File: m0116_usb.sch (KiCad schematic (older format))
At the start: 20 parts, among them J1 AVR-ISP-6, J2 USB_B_Mini, U1 ATmega32A-PU, Y1 16Mhz

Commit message: finished
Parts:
- removed D82: LED, LED_THT:LED_D3.0mm, symbol Device:LED
- removed R4: 1.5k, Resistor_THT:R_Axial_DIN0207_L6.3mm_D2.5mm_P10.16mm_Horizontal, symbol Device:R
- added D10, D11, D12, D13, D14, D15, D16, D17, D18, D19, D20, D21, D22, D23, D24, D25, D26, D27, D28, D29, D3, D30, D31, D32, D33, D34, D35, D36, D37, D38, D39, D4, D40, D41, D42, D43, D44, D45, D46, D47, D48, D49, D5, D50, D51, D52, D53, D54, D55, D56, D57, D58, D59, D6, D60, D61, D62, D63, D64, D65, D66, D67, D68, D69, D7, D70, D71, D72, D73, D74, D75, D76, D77, D78, D79, D8, D80, D81, D83, D84, D9: D_Small, Diode_THT:D_DO-35_SOD27_P7.62mm_Horizontal, symbol Device:D_Small
- added J3, J4: Conn_01x04, Connector_PinHeader_2.54mm:PinHeader_1x04_P2.54mm_Vertical, symbol Connector_Generic:Conn_01x04
- added J5, J6: Conn_01x06, Connector_PinHeader_2.54mm:PinHeader_1x06_P2.54mm_Vertical, symbol Connector_Generic:Conn_01x06
- added MX1, MX10, MX11, MX12, MX13, MX14, MX15, MX16, MX17, MX18, MX19, MX2, MX20, MX21, MX22, MX23, MX24, MX25, MX26, MX27, MX28, MX29, MX3, MX30, MX31, MX32, MX33, MX34, MX35, MX36, MX37, MX38, MX39, MX4, MX40, MX41, MX42, MX43, MX44, MX45, MX46, MX47, MX48, MX49, MX5, MX50, MX51, MX52, MX53, MX54, MX55, MX56, MX57, MX58, MX59, MX6, MX60, MX61, MX62, MX63, MX64, MX65, MX66, MX67, MX68, MX69, MX7, MX70, MX71, MX72, MX73, MX74, MX75, MX76, MX77, MX78, MX79, MX8, MX80, MX81, MX9: MX-NoLED, Alps_Only:ALPS-1U, symbol MX_Alps_Hybrid:MX-NoLED
- F1: footprint custom_parts:Fuse_Littelfuse_395Series -> Fuse:Fuse_Littelfuse_395Series
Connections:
- net +5V: now also R5.2, J3.1 (Pin_1), J4.1 (Pin_1), J5.6 (Pin_6), J6.6 (Pin_6); no longer R5.1
- net D+: now also R3.2; no longer R2.2
- net D-: now also R2.2; no longer R3.2
- net GND: now also J3.4 (Pin_4), J4.4 (Pin_4), J5.1 (Pin_1), J6.1 (Pin_1)
- net MISO: now also J6.4 (Pin_4); no longer J1.1 (MISO)
- net MOSI: now also J6.5 (Pin_5); no longer J1.4 (MOSI)
- net SCK: now also J6.3 (Pin_3); no longer J1.3 (SCK)
- net reset: now also J6.2 (Pin_2); no longer J1.5 (~RST)
- net col4: now reaches U1.14 (PD0)
- net col4: now also MX22.1 (COL), MX4.1 (COL), MX40.1 (COL), MX56.1 (COL), MX71.1 (COL)
- net col3: now reaches U1.15 (PD1)
- net col3: now also MX21.1 (COL), MX3.1 (COL), MX39.1 (COL), MX55.1 (COL), MX70.1 (COL)
- net col2: now reaches U1.19 (PD5)
- net col2: now also MX2.1 (COL), MX20.1 (COL), MX38.1 (COL), MX54.1 (COL), MX69.1 (COL)
- net row0: now reaches U1.2 (PB1)
- net row0: now also D10.1 (K), D11.1 (K), D12.1 (K), D13.1 (K), D14.1 (K), D15.1 (K), D16.1 (K), D17.1 (K), D18.1 (K), D19.1 (K), D20.1 (K), D3.1 (K), D4.1 (K), D5.1 (K), D6.1 (K), D7.1 (K), D8.1 (K), D9.1 (K)
- net col1: now reaches U1.20 (PD6)
- net col1: now also MX1.1 (COL), MX19.1 (COL), MX37.1 (COL), MX53.1 (COL), MX68.1 (COL)
- net col5: now reaches U1.21 (PD7)
- net col5: now also MX23.1 (COL), MX41.1 (COL), MX5.1 (COL), MX57.1 (COL)
- net col6: now reaches U1.22 (PC0)
- net col6: now also MX24.1 (COL), MX42.1 (COL), MX58.1 (COL), MX6.1 (COL), MX81.1 (COL)
- net col7: now reaches U1.23 (PC1)
- net col7: now also MX25.1 (COL), MX43.1 (COL), MX59.1 (COL), MX7.1 (COL)
- net col8: now reaches U1.24 (PC2)
- net col8: now also MX26.1 (COL), MX44.1 (COL), MX60.1 (COL), MX72.1 (COL), MX8.1 (COL)
- net col9: now reaches U1.25 (PC3)
- net col9: now also MX27.1 (COL), MX45.1 (COL), MX61.1 (COL), MX73.1 (COL), MX9.1 (COL)
- net col10: now reaches U1.26 (PC4)
- net col10: now also MX10.1 (COL), MX28.1 (COL), MX46.1 (COL), MX62.1 (COL), MX74.1 (COL)
- net col11: now reaches U1.27 (PC5)
- net col11: now also MX11.1 (COL), MX29.1 (COL), MX47.1 (COL), MX63.1 (COL), MX75.1 (COL)
- net col12: now reaches U1.28 (PC6)
- net col12: now also MX12.1 (COL), MX30.1 (COL), MX48.1 (COL), MX76.1 (COL)
- net col13: now reaches U1.29 (PC7)
- net col13: now also MX13.1 (COL), MX31.1 (COL)
- net row2: now reaches U1.3 (PB2)
- net row2: now also D39.1 (K), D40.1 (K), D41.1 (K), D42.1 (K), D43.1 (K), D44.1 (K), D45.1 (K), D46.1 (K), D47.1 (K), D48.1 (K), D49.1 (K), D50.1 (K), D51.1 (K), D52.1 (K), D53.1 (K), D54.1 (K)
- net col14: now reaches U1.33 (PA7)
- net col14: now also MX14.1 (COL), MX32.1 (COL), MX64.1 (COL), MX77.1 (COL)
- net col15: now reaches U1.34 (PA6)
- net col15: now also MX15.1 (COL), MX33.1 (COL), MX49.1 (COL), MX65.1 (COL), MX78.1 (COL)
- net col16: now reaches U1.35 (PA5)
- net col16: now also MX16.1 (COL), MX34.1 (COL), MX50.1 (COL), MX66.1 (COL)
- net col17: now reaches U1.36 (PA4)
- net col17: now also MX17.1 (COL), MX35.1 (COL), MX51.1 (COL), MX67.1 (COL), MX79.1 (COL)
- net col18: now reaches U1.37 (PA3)
- net col18: now also MX18.1 (COL), MX36.1 (COL), MX52.1 (COL), MX80.1 (COL)
- net row3: now reaches U1.38 (PA2)
- net row3: now also D55.1 (K), D56.1 (K), D57.1 (K), D58.1 (K), D59.1 (K), D60.1 (K), D61.1 (K), D62.1 (K), D63.1 (K), D64.1 (K), D65.1 (K), D66.1 (K), D67.1 (K), D68.1 (K), D69.1 (K)
- net row4: now reaches U1.39 (PA1)
- net row4: now also D70.1 (K), D71.1 (K), D72.1 (K), D73.1 (K), D74.1 (K), D75.1 (K), D76.1 (K), D77.1 (K), D78.1 (K), D79.1 (K), D80.1 (K), D81.1 (K), D83.1 (K), D84.1 (K)
- net row1: now reaches U1.40 (PA0)
- net row1: now also D21.1 (K), D22.1 (K), D23.1 (K), D24.1 (K), D25.1 (K), D26.1 (K), D27.1 (K), D28.1 (K), D29.1 (K), D30.1 (K), D31.1 (K), D32.1 (K), D33.1 (K), D34.1 (K), D35.1 (K), D36.1 (K), D37.1 (K), D38.1 (K)
- net at D2.1 (K), J2.2 (D-): now also J4.3 (Pin_3); no longer R3.1
- net at D1.1 (K), J2.3 (D+): now also J4.2 (Pin_2); no longer R2.1, R5.2
- new net: J3.2 (Pin_2), R3.1
- new net: J3.3 (Pin_3), R2.1, R5.1
- new net: D3.2 (A), MX1.2 (ROW)
- new net: D4.2 (A), MX2.2 (ROW)
- new net: D5.2 (A), MX3.2 (ROW)
- new net: D6.2 (A), MX4.2 (ROW)
- new net: D7.2 (A), MX5.2 (ROW)
- new net: D8.2 (A), MX6.2 (ROW)
- new net: D9.2 (A), MX7.2 (ROW)
- new net: D10.2 (A), MX8.2 (ROW)
- new net: D11.2 (A), MX9.2 (ROW)
- new net: D12.2 (A), MX10.2 (ROW)
- new net: D13.2 (A), MX11.2 (ROW)
- new net: D14.2 (A), MX12.2 (ROW)
- new net: D15.2 (A), MX13.2 (ROW)
- new net: D16.2 (A), MX14.2 (ROW)
- new net: D17.2 (A), MX15.2 (ROW)
- new net: D18.2 (A), MX16.2 (ROW)
- new net: D19.2 (A), MX17.2 (ROW)
- new net: D20.2 (A), MX18.2 (ROW)
- new net: D21.2 (A), MX19.2 (ROW)
- new net: D22.2 (A), MX20.2 (ROW)
- new net: D23.2 (A), MX21.2 (ROW)
- new net: D24.2 (A), MX22.2 (ROW)
- new net: D25.2 (A), MX23.2 (ROW)
- new net: D26.2 (A), MX24.2 (ROW)
- new net: D27.2 (A), MX25.2 (ROW)
- new net: D28.2 (A), MX26.2 (ROW)
- new net: D29.2 (A), MX27.2 (ROW)
- new net: D30.2 (A), MX28.2 (ROW)
- new net: D31.2 (A), MX29.2 (ROW)
- new net: D32.2 (A), MX30.2 (ROW)
- new net: D33.2 (A), MX31.2 (ROW)
- new net: D34.2 (A), MX32.2 (ROW)
- new net: D35.2 (A), MX33.2 (ROW)
- new net: D36.2 (A), MX34.2 (ROW)
- new net: D37.2 (A), MX35.2 (ROW)
- new net: D38.2 (A), MX36.2 (ROW)
- new net: D39.2 (A), MX37.2 (ROW)
- new net: D40.2 (A), MX38.2 (ROW)
- new net: D41.2 (A), MX39.2 (ROW)
- new net: D42.2 (A), MX40.2 (ROW)
- new net: D43.2 (A), MX41.2 (ROW)
- new net: D44.2 (A), MX42.2 (ROW)
- new net: D45.2 (A), MX43.2 (ROW)
- new net: D46.2 (A), MX44.2 (ROW)
- new net: D47.2 (A), MX45.2 (ROW)
- new net: D48.2 (A), MX46.2 (ROW)
- new net: D49.2 (A), MX47.2 (ROW)
- new net: D50.2 (A), MX48.2 (ROW)
- new net: D51.2 (A), MX49.2 (ROW)
- new net: D52.2 (A), MX50.2 (ROW)
- new net: D53.2 (A), MX51.2 (ROW)
- new net: D54.2 (A), MX52.2 (ROW)
- new net: D55.2 (A), MX53.2 (ROW)
- new net: D56.2 (A), MX54.2 (ROW)
- new net: D57.2 (A), MX55.2 (ROW)
- new net: D58.2 (A), MX56.2 (ROW)
- new net: D59.2 (A), MX57.2 (ROW)
- new net: D60.2 (A), MX58.2 (ROW)
- new net: D61.2 (A), MX59.2 (ROW)
- new net: D62.2 (A), MX60.2 (ROW)
- new net: D63.2 (A), MX61.2 (ROW)
- new net: D64.2 (A), MX62.2 (ROW)
- new net: D65.2 (A), MX63.2 (ROW)
- new net: D66.2 (A), MX64.2 (ROW)
- new net: D67.2 (A), MX65.2 (ROW)
- new net: D68.2 (A), MX66.2 (ROW)
- new net: D69.2 (A), MX67.2 (ROW)
- new net: D70.2 (A), MX68.2 (ROW)
- new net: D71.2 (A), MX69.2 (ROW)
- new net: D72.2 (A), MX70.2 (ROW)
- new net: D73.2 (A), MX71.2 (ROW)
- new net: D74.2 (A), MX72.2 (ROW)
- new net: D75.2 (A), MX73.2 (ROW)
- new net: D76.2 (A), MX74.2 (ROW)
- new net: D77.2 (A), MX75.2 (ROW)
- new net: D78.2 (A), MX76.2 (ROW)
- new net: D79.2 (A), MX77.2 (ROW)
- new net: D80.2 (A), MX78.2 (ROW)
- new net: D81.2 (A), MX79.2 (ROW)
- new net: D83.2 (A), MX80.2 (ROW)
- new net: D84.2 (A), MX81.2 (ROW)
- new net: J1.1 (MISO), J5.4 (Pin_4)
- new net: J1.3 (SCK), J5.3 (Pin_3)
- new net: J1.4 (MOSI), J5.5 (Pin_5)
- new net: J1.5 (~RST), J5.2 (Pin_2)
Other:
- moved on the sheet: F1, R2, R3, R5

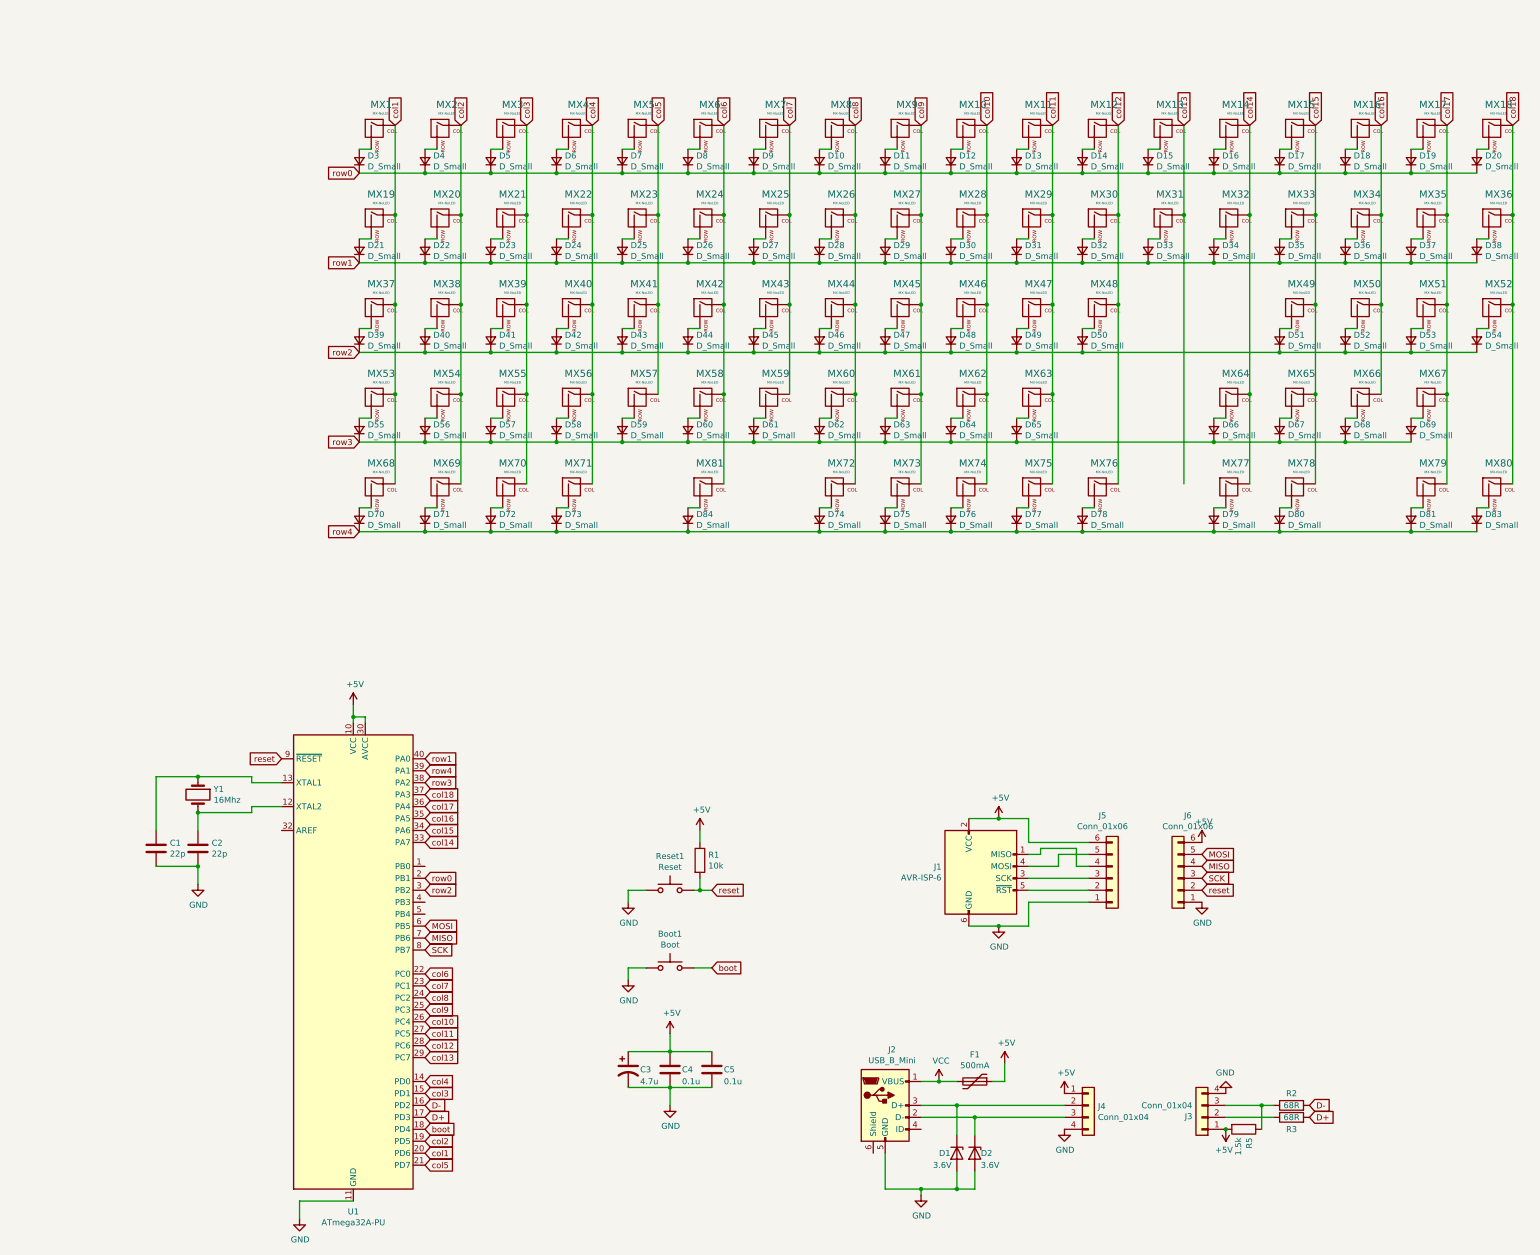
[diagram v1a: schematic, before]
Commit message: fix wrong resistor connection
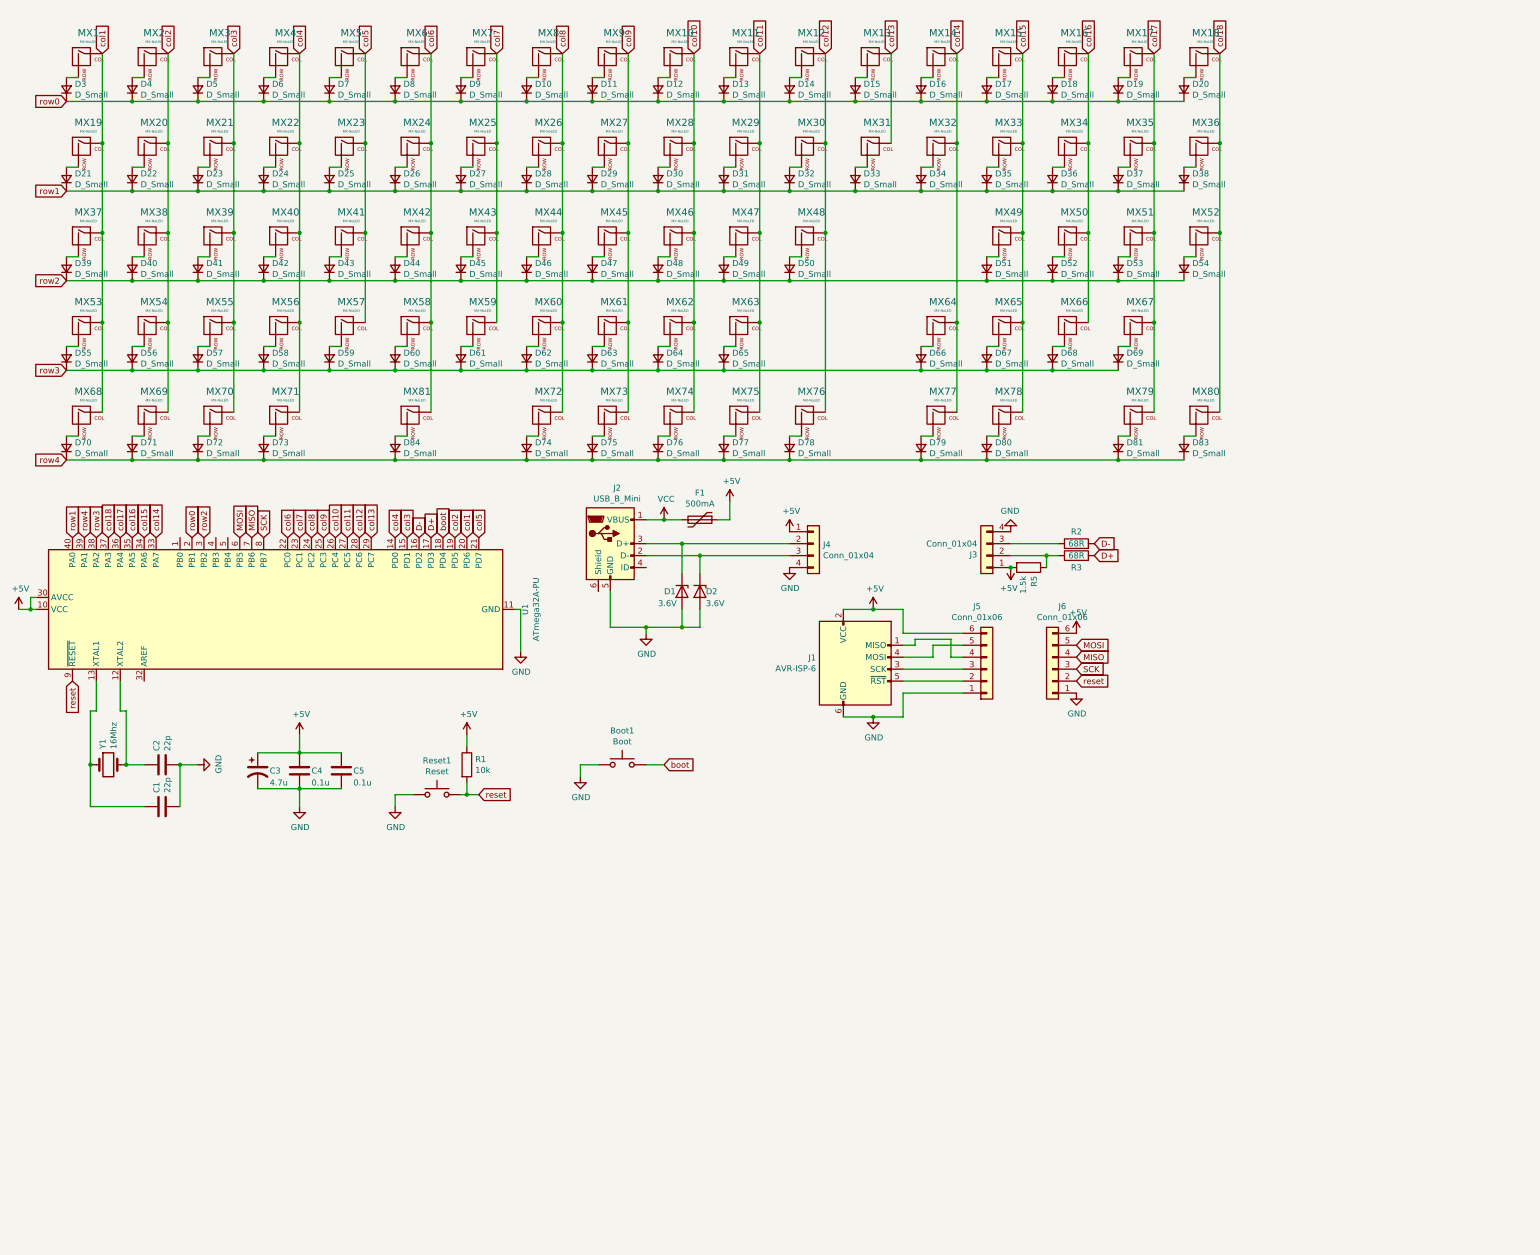
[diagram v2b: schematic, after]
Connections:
- net at J3.2 (Pin_2), R3.1: now also R5.1
- net at J3.3 (Pin_3), R2.1: no longer R5.1
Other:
- moved on the sheet: Boot1, C1, C2, C3, C4, C5, D1, D10, D11, D12, D13, D14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

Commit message: rev1
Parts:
- removed C1, C2: 22p, Capacitor_THT:C_Disc_D6.0mm_W2.5mm_P5.00mm, symbol Device:C
- removed J5, J6: Conn_01x06, Connector_PinHeader_2.54mm:PinHeader_1x06_P2.54mm_Vertical, symbol Connector_Generic:Conn_01x06
- removed Y1: 16Mhz, Crystal:Crystal_HC49-4H_Vertical, symbol Device:Crystal
- added Y1: Resonator, Crystal:Resonator-3Pin_W7.0mm_H2.5mm, symbol Device:Resonator
- renumbered C3 to C1, C4 to C2, C5 to C3, D84 to D74, D74 to D75, D75 to D76, D76 to D77, D77 to D78, D78 to D79, D79 to D80, D80 to D81, D81 to D82, J4 to J2, MX81 to MX72, MX72 to MX73, MX73 to MX74, MX74 to MX75, MX75 to MX76, MX76 to MX77, MX77 to MX78, MX78 to MX79, MX79 to MX80, MX80 to MX81, R5 to R2, R2 to R4, J2 to USB1
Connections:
- net D+: now also U1.16 (PD2); no longer U1.17 (PD3)
- net D-: now also U1.17 (PD3); no longer U1.16 (PD2)
- net GND: now also USB1.6 (Shield), Y1.2
- net MISO: now also J1.1 (MISO)
- net MOSI: now also J1.4 (MOSI)
- net SCK: now also J1.3 (SCK)
- net reset: now also J1.5 (~RST)
- net at U1.12 (XTAL2): now also Y1.3
- net at U1.13 (XTAL1): now also Y1.1
- net at J3.2 (Pin_2), R3.1: no longer R2.1
- net at J3.3 (Pin_3), R4.1: now also R2.1
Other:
- moved on the sheet: J1, J3, R2, R3, R4

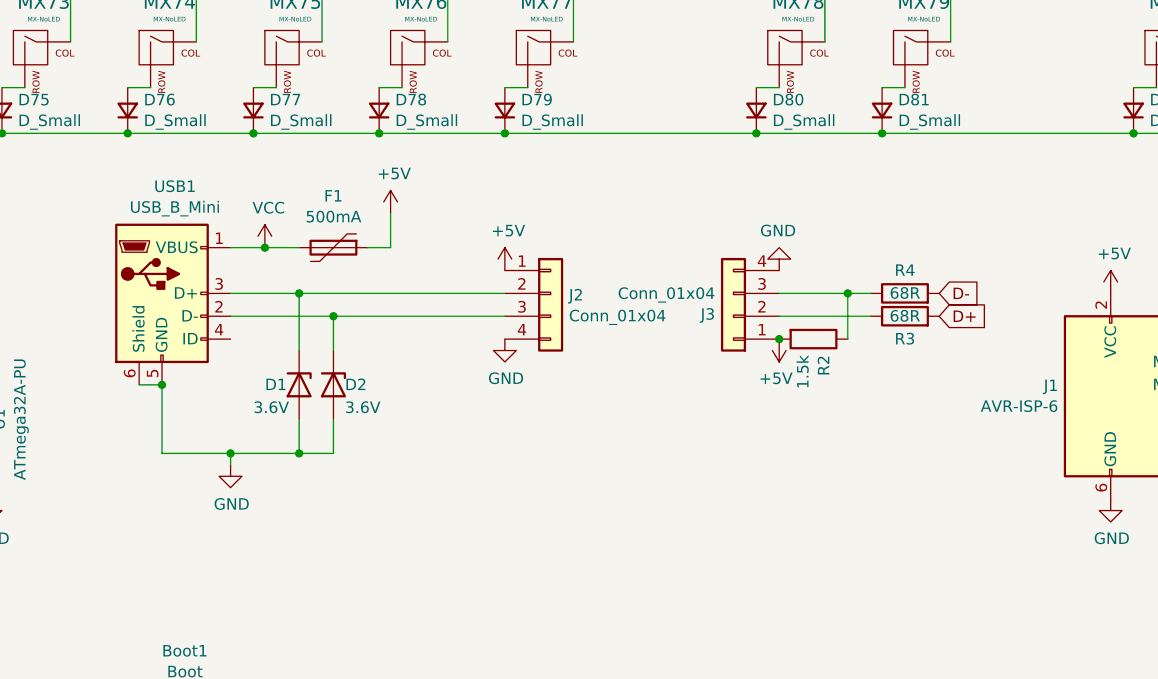
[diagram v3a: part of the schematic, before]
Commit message: change design of daughterboard
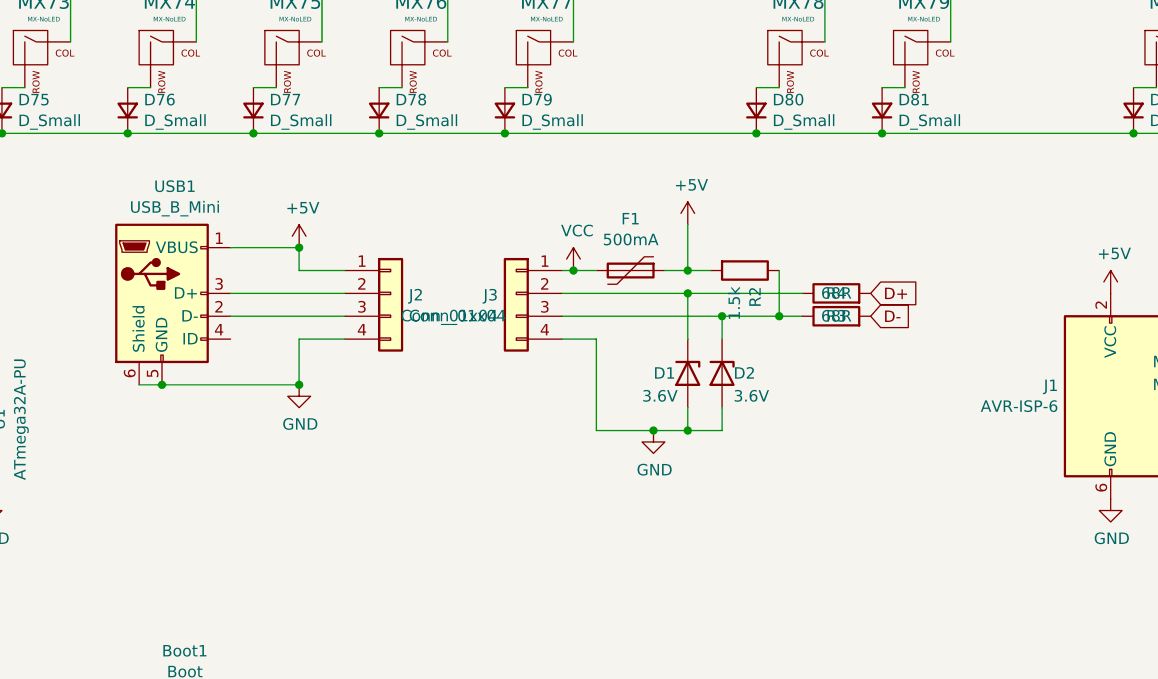
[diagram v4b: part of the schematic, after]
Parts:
- J2: footprint Connector_PinHeader_2.54mm:PinHeader_1x04_P2.54mm_Vertical -> Connector_PinHeader_2.00mm:PinHeader_1x04_P2.00mm_Vertical
- J3: footprint Connector_PinHeader_2.54mm:PinHeader_1x04_P2.54mm_Vertical -> Connector_JST:JST_EH_B4B-EH-A_1x04_P2.50mm_Vertical
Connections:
- net +5V: now also USB1.1 (VBUS); no longer J3.1 (Pin_1)
- net VCC: now also J3.1 (Pin_1); no longer USB1.1 (VBUS)
- net at J3.2 (Pin_2), R3.1: now also D1.1 (K)
- net at J3.3 (Pin_3), R2.1, R4.1: now also D2.1 (K)
- net at J2.2 (Pin_2), USB1.3 (D+): no longer D1.1 (K)
- net at J2.3 (Pin_3), USB1.2 (D-): no longer D2.1 (K)
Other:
- moved on the sheet: D1, D2, F1, J2, J3, R2, R3, R4
